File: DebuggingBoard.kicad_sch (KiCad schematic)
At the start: 31 parts, among them J1 Conn_01x05_Socket, SW1 SW_SPDT, U1 STM32F373CCTx, U2 LT8609SIV_PBF, Y1 16MHz

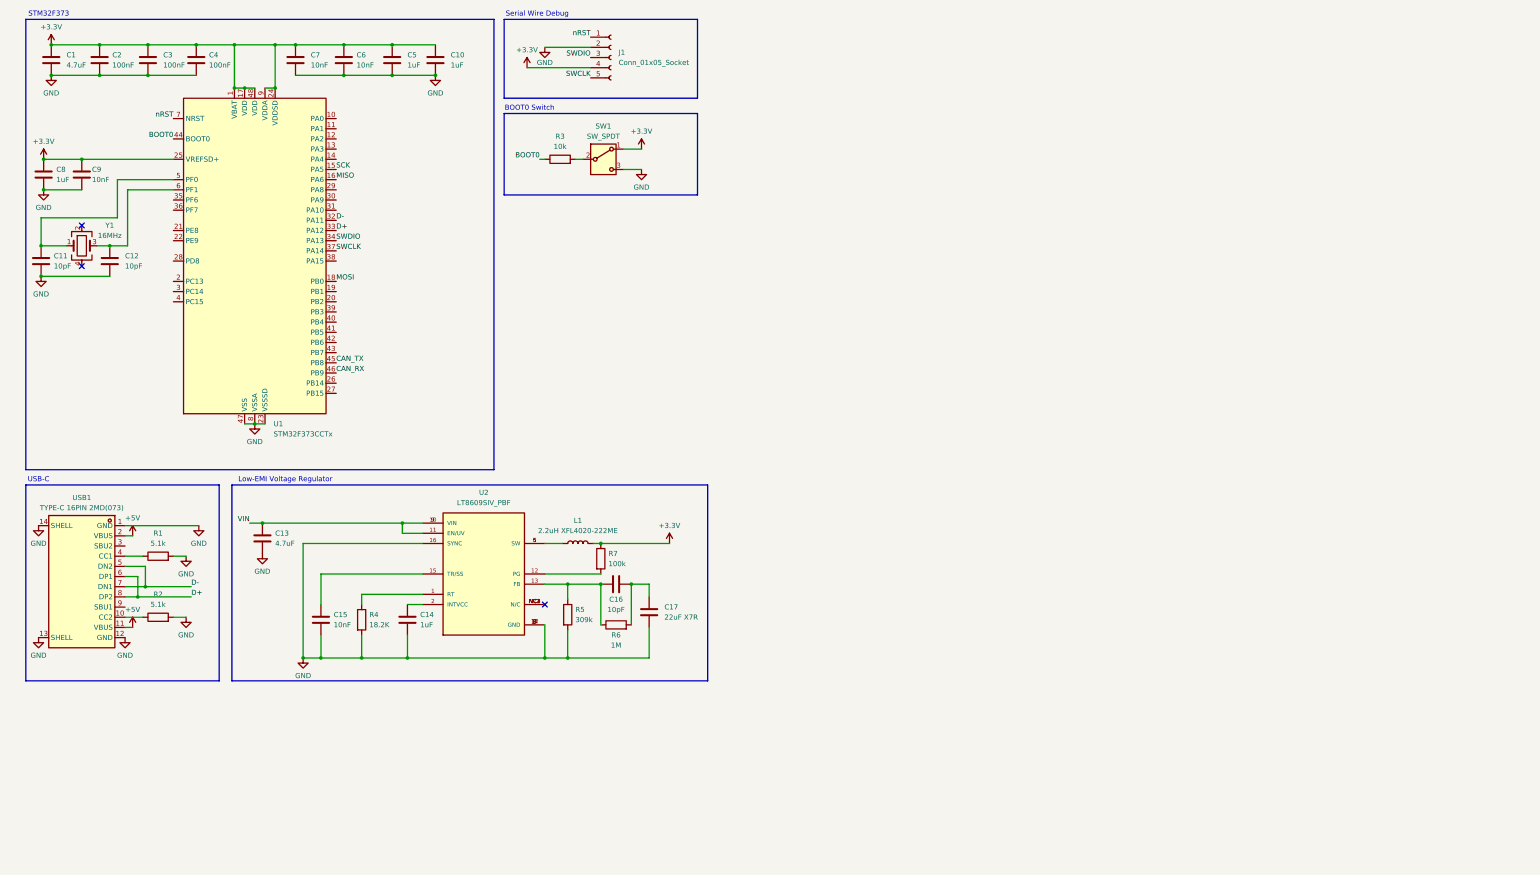
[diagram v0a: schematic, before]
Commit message: added sim files and osc
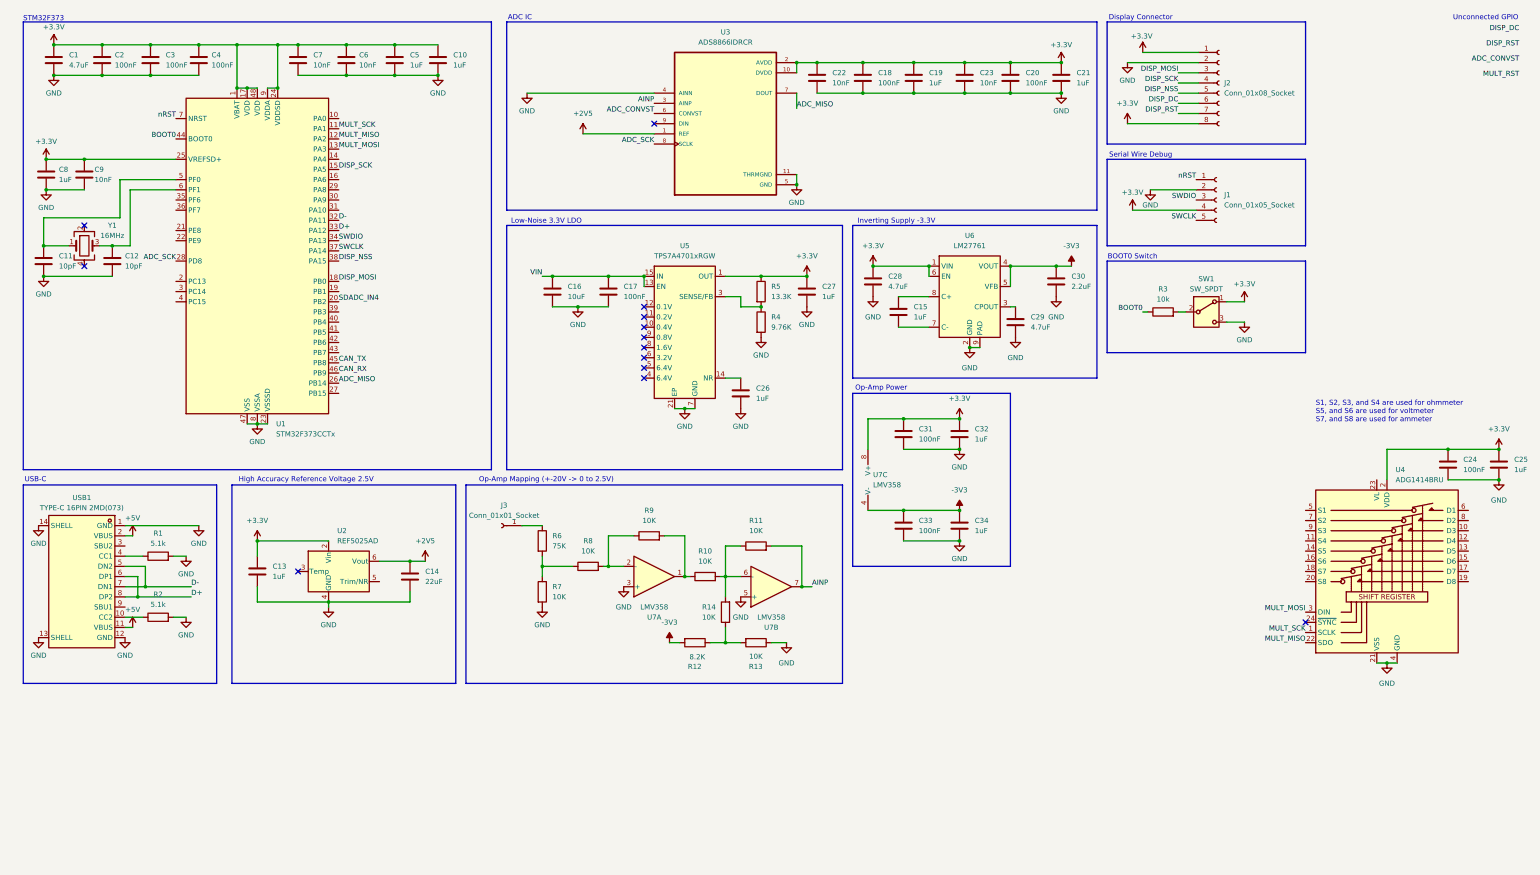
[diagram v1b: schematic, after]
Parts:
- removed L1: 2.2uH XFL4020-222ME, symbol Device:L
- removed U2: LT8609SIV_PBF, LT8609SIV_PBF:REG_LT8609SIV_PBF, symbol LT8609S:LT8609SIV_PBF
- added C18, C20, C24, C31, C33: 100nF, symbol Device:C
- added C19, C21, C25, C26, C27, C32, C34: 1uF, symbol Device:C
- added C22, C23: 10nF, symbol Device:C
- added C28, C29: 4.7uF, symbol Device:C
- added C30: 2.2uF, symbol Device:C
- added J2: Conn_01x08_Socket, symbol Connector:Conn_01x08_Socket
- added J3: Conn_01x01_Socket, symbol Connector:Conn_01x01_Socket
- added R10, R11, R13, R14, R8, R9: 10K, symbol Device:R
- added R12: 8.2K, symbol Device:R
- added U2: REF5025AD, Package_SO:SOIC-8_3.9x4.9mm_P1.27mm, symbol Reference_Voltage:REF5025AD
- added U3: ADS8866IDRCR, ADS8866IDRCR:VREG_V62_16624-01YE, symbol ADS8866:ADS8866IDRCR
- added U4: ADG1414BRU, Package_SO:TSSOP-24_4.4x7.8mm_P0.65mm, symbol Analog_Switch:ADG1414BRU
- added U5: TPS7A4701xRGW, Package_DFN_QFN:Texas_RGW0020A_VQFN-20-1EP_5x5mm_P0.65mm_EP3.15x3.15mm_ThermalVias, symbol Regulator_Linear:TPS7A4701xRGW
- added U6: LM27761, Package_SON:WSON-8-1EP_2x2mm_P0.5mm_EP0.9x1.6mm, symbol Regulator_SwitchedCapacitor:LM27761
- added U7: LMV358, symbol Amplifier_Operational:LMV358
- C13: value 4.7uF -> 1uF
- C14: value 1uF -> 22uF
- C15: value 10nF -> 1uF
- C16: value 10pF -> 10uF
- C17: value 22uF X7R -> 100nF
- R4: value 18.2K -> 9.76K
- R5: value 309k -> 13.3K
- R6: value 1M -> 75K
- R7: value 100k -> 10K
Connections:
- net +3.3V: now also C13.1, R5.1, C18.1, C19.1, C20.1, C21.1, C22.1, C23.1, C24.1, C25.1, C27.1, C28.1, C31.1, C32.1, J2.1 (Pin_1), J2.8 (Pin_8), U2.2 (Vin), U3.10 (DVDD), U3.2 (AVDD), U4.2 (VDD), U5.1 (OUT), U5.20 (OUT), U6.1 (VIN), U6.6 (EN), U7.8 (V+); no longer R7.1
- net GND: now also C16.2, C17.2, R7.2, C18.2, C19.2, C20.2, C21.2, C22.2, C23.2, C24.2, C25.2, C26.2, C27.2, C28.2, C29.2, C30.2, C31.2, C32.2, C33.2, C34.2, J2.2 (Pin_2), R13.1, U2.4 (GND), U3.11 (THRMGND), U3.4 (AINN), U3.5 (GND), U4.21 (VSS), U4.4 (GND), U5.21 (EP), U5.7 (GND), U6.2 (GND), U6.9 (PAD), U7.3 (+), U7.5 (+); no longer C15.2, C17.1, R5.2
- net VIN: now also C16.1, C17.1, U5.13 (EN), U5.15 (IN), U5.16 (IN); no longer C13.1
- net at R4.1: now also R5.2, U5.3 (SENSE/FB)
- net at C15.1: now also U6.8 (C+)
- net +2V5: now reaches C14.1
- net +2V5: now also U2.6 (Vout), U3.1 (REF)
- net MULT_SCK: now reaches U1.11 (PA1)
- net MULT_SCK: now also U4.1 (SCLK)
- net MULT_MISO: now reaches U1.12 (PA2)
- net MULT_MISO: now also U4.22 (SDO)
- net MULT_MOSI: now reaches U1.13 (PA3)
- net MULT_MOSI: now also U4.3 (DIN)
- net SDADC_IN4: now reaches U1.20 (PB2)
- net ADC_MISO: now reaches U1.26 (PB14)
- net ADC_MISO: now also U3.7 (DOUT)
- net ADC_SCK: now reaches U1.28 (PD8)
- net ADC_SCK: now also U3.8 (SCLK)
- net DISP_NSS: now reaches U1.38 (PA15)
- net DISP_NSS: now also J2.5 (Pin_5)
- net MISO: no longer names the net of U1.16 (PA6)
- net MOSI renamed DISP_MOSI
- net DISP_MOSI: now also J2.3 (Pin_3)
- net SCK renamed DISP_SCK
- net DISP_SCK: now also J2.4 (Pin_4)
- new net: C15.2, U6.7 (C-)
- new net: R12.1, R13.2, R14.1
- new net: C29.1, U6.3 (CPOUT)
- new net: J3.1 (Pin_1), R6.1
- new net: R6.2, R7.1, R8.1
- new net: R10.2, R11.1, R14.2, U7.6 (-)
- new net: R8.2, R9.1, U7.2 (-)
- new net: R10.1, R9.2, U7.1
- new net: C26.1, U5.14 (NR)
- new net -3V3: C30.1, C33.1, C34.1, R12.2, U6.4 (VOUT), U6.5 (VFB), U7.4 (V-)
- new net ADC_CONVST: U3.6 (CONVST)
- new net AINP: R11.2, U3.3 (AINP), U7.7
- new net DISP_DC: J2.6 (Pin_6)
- new net DISP_RST: J2.7 (Pin_7)
- no-connect marks 3 -> 13
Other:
- note added: "ADC IC"
- note added: "Display Connector"
- note added: "High Accuracy Reference Voltage 2.5V"
- note added: "Inverting Supply -3.3V"
- note added: "Low-Noise 3.3V LDO"
- note added: "Op-Amp Mapping (+-20V -> 0 to 2.5V)"
- note added: "Op-Amp Power"
- note added: "S1, S2, S3, and S4 are used for ohmmeter S5, and S6 are used for voltmeter S7, and S8 are used for ammeter"
- note added: "Unconnected GPIO"
- note removed: "Low-EMI Voltage Regulator"
- moved on the sheet: C1, C10, C11, C12, C2, C3, C4, C5, C6, C7, C8, C9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

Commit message: nearly final osc
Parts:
- removed C13, C27: 1uF, symbol Device:C
- removed C14: 22uF, symbol Device:C
- removed U2: REF5025AD, Package_SO:SOIC-8_3.9x4.9mm_P1.27mm, symbol Reference_Voltage:REF5025AD
- removed U3: ADS8866IDRCR, ADS8866IDRCR:VREG_V62_16624-01YE, symbol ADS8866:ADS8866IDRCR
- removed U5: TPS7A4701xRGW, Package_DFN_QFN:Texas_RGW0020A_VQFN-20-1EP_5x5mm_P0.65mm_EP3.15x3.15mm_ThermalVias, symbol Regulator_Linear:TPS7A4701xRGW
- removed U7: LMV358, symbol Amplifier_Operational:LMV358
- added C13: 100n, Capacitor_SMD:C_0402_1005Metric, symbol Device:C
- added C13: 10uF, Capacitor_SMD:C_0603_1608Metric, symbol Device:C
- added C14 (x2): 22uF, Capacitor_SMD:C_0805_2012Metric, symbol Device:C
- added C35: 680pF, symbol Device:C
- added D1, D2: D, symbol Device:D
- added F1: Fuse, symbol Device:Fuse
- added L1: FNR5020S3R3NT, Rocketry_Easyeda:IND-SMD_L5.0-W5.0_FNR50XXS, symbol Rocketry:FNR5020S3R3NT
- added R15, R16, R17: 33R, symbol Device:R
- added R18: 10K, Resistor_SMD:R_0402_1005Metric, symbol Device:R
- added R19: 37.4K, Resistor_SMD:R_0402_1005Metric, symbol Device:R
- added R20, R23: 100K, symbol Device:R
- added R21: 10M, symbol Device:R
- added R22: 316K, symbol Device:R
- added R24: 12.4K, symbol Device:R
- added R25: 187K, symbol Device:R
- added R26: 22.1K, symbol Device:R
- added R27: 1M, symbol Device:R
- added RV1: Varistor, symbol Device:Varistor
- added U2: AP62300TWU, Package_TO_SOT_SMD:TSOT-23-6, symbol Regulator_Switching:AP62300TWU
- added U3: ADS7056IRUGR, Rocketry_Easyeda:X2QFN-8_L1.5-W1.5-P0.50-BL, symbol ROCKETRY_EASYEDA:ADS7056IRUGR
- added U7: OPA2156xD, Package_SO:SOIC-8_3.9x4.9mm_P1.27mm, symbol Amplifier_Operational:OPA2156xD
- added U8: TPS7A9401DSCR, Rocketry_Easyeda:WSON-10_L3.0-W3.0-P0.50-TL-EP, symbol ROCKETRY_EASYEDA:TPS7A9401DSCR
- C17: value 100nF -> 10uF
- C18: value 100nF -> 1uF
- C19: value 1uF -> 100nF
- C26: value 1uF -> 4.7uF
- R10, R11, R13, R14: value 10K -> 20K
- R12: value 8.2K -> 10K
- R4: value 9.76K -> 10M
- R5: value 13.3K -> 1M
- R6: value 75K -> 56.2K
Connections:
- net +3.3V: now also C17.1, R25.2, U3.4 (DVDD), U3.6 (AVDD), U7.8 (V+), U8.10 (OUT), U8.8 (SNS), U8.9 (OUT); no longer J2.1 (Pin_1), R5.1
- net -3V3: now also U7.4 (V-)
- net ADC_CONVST: now also R17.1
- net ADC_MISO: now also R16.1
- net ADC_SCK: now also R15.1
- net AINP: now also C35.2, U3.7 (AINP), U7.7
- net GND: now also C13.2, C14.2, C14.2, C35.1, D1.1 (K), D2.2 (A), F1.1, R18.1, R20.1, R23.2, R26.2, R27.1, U2.1 (GND), U3.5 (GND), U3.8 (AINM), U7.3 (+), U7.5 (+), U8.11 (EP), U8.6 (GND); no longer R4.2
- net VIN: now also C13.1, U2.3 (IN); no longer C16.1, C17.1
- net S5: now reaches R4.1, R5.2
- net S5: now also U4.14 (S5)
- net at R10.2, R11.1, R14.2: now also U7.6 (-)
- net at R8.2, R9.1: now also U7.2 (-)
- net at R10.1, R9.2: now also U7.1
- net at C26.1: now also R26.1, U8.7 (NR/SS)
- net MULT_+: now reaches U4.11 (S4)
- net MULT_+: now also R4.2, D1.2 (A), D2.1 (K), R21.2, RV1.1
- net Voltmeter_OUT: now reaches U4.12 (D4)
- net Voltmeter_OUT: now also U4.13 (D5), U4.15 (D6), U4.17 (D7)
- net S6: now reaches U4.16 (S6)
- net S6: now also R5.1, F1.2, R20.2, RV1.2
- new net: R24.2, R25.1, U8.5 (FB_PG)
- new net: R17.2, U3.1 (~{CS})
- new net: R16.2, U3.2 (SDO)
- new net: R15.2, U3.3 (SCLK)
- new net: R22.2, R23.1, U8.3 (EN_UV)
- new net: R24.1, U8.4 (PG)
- new net BST1: C13.1, U2.6 (BST)
- new net FB1: R18.2, R19.2, U2.4 (FB)
- new net LDO_VIN: C14.1, C14.1, C16.1, J2.1 (Pin_1), L1.2, R19.1, R22.1, U8.1 (IN), U8.2 (IN)
- new net S8: R21.1, R27.2
- new net SW1: C13.2, L1.1, U2.2 (SW)
- no-connect marks 13 -> 3
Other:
- note added: "0-3.6V"
- note added: "0-360V"
- note added: "0-36V"
- note added: "3.6V Switching Voltage Regulator"
- note added: "Multimeter Stuffs"
- note added: "Op-Amp Power Supply"
- note added: "S1, S2, and S3 are used for ohmmeter S4, S5, and S6 are used for voltmeter S7, and S8 is used for ammeter"
- note removed: "High Accuracy Reference Voltage 2.5V"
- note removed: "Op-Amp Power"
- note removed: "S1, S2, S3, and S4 are used for ohmmeter S5, and S6 are used for voltmeter S7, and S8 are used for ammeter"
- moved on the sheet: C1, C10, C15, C2, C20, C21, C23, C24, C25, C28, C29, C3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
